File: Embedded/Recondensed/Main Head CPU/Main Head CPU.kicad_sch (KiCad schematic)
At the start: 52 parts, among them J1 10171746-00021LF, J10 Fan 1, J11 Substructure Power, J12 Head Power, J13 MicroSD, J14 Mic, J15 Expansion, J2 LEDs 0, J3 LEDs 1, J4 LEDs 2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

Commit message: Added LCSC Component IDs
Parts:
- removed SW1: Boot, Buttons:R-667843, symbol Switch:SW_Push
- removed SW2: RST, Buttons:R-667843, symbol Switch:SW_Push
- added S1: Boot, Buttons:SW_B3U-1000P, symbol Buttons:B3U-1000P
- added S2: RST, Buttons:SW_B3U-1000P, symbol Buttons:B3U-1000P
- C1, C4, C5: LCSC (none) -> C3039698
- C10, C2, C3, C8: LCSC (none) -> C1591
- C6: LCSC (none) -> C95843
- C7, C9: LCSC (none) -> C84419
- D1, D2: LCSC (none) -> C7207730
- D3: LCCS (none) -> C50603
- J1: footprint USBC:AMPHENOL_10171746-00021LF -> USBC:MOLEX_2171790001; LCSC (none) -> C3197684
- J10, J9: LCSC (none) -> C189893
- J13: LCSC (none) -> C587826
- J14, J15, J8: LCSC (none) -> C265111
- J2, J3, J4, J5, J6, J7: LCSC (none) -> C514175
- R1, R2: LCSC (none) -> C328432
- R10, R11, R12, R13, R14, R3, R5, R9: LCSC (none) -> C98220
- R7: value 155ohm min -> 145ohm; LCSC (none) -> C2930065
- R8: value 70ohm min -> 33ohm; LCSC (none) -> C108661
- U3: LCSC (none) -> C86781
- U4: LCSC (none) -> C134077
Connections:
- net GND: now also J1.A1B12 (GND_A), J1.B1A12 (GND_B), S1.2, S2.1; no longer J1.A1_B12 (GND_A), J1.B1_A12 (GND_B)
- net at C1.1, D3.A: now also J1.A4B9 (VBUS_A), J1.B4A9 (VBUS_B); no longer J1.A4_B9 (VBUS_A), J1.B4_A9 (VBUS_B)
- net at ESP1.27 (GPIO0/BOOT), R10.2: now also S1.1
- net at C6.2, ESP1.3 (EN), R9.2: now also S2.2
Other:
- moved on the sheet: J10, J9, Q1, Q2, R4, R6

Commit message: Modified Tables per component to centralise LCSC IDs
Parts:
- D3: LCCS C50603 -> (none); LCSC (none) -> C50603
- ESP1, J11, J12, U5: now left out of the parts list
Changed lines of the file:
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@@
 		(unit 1)
 		(exclude_from_sim no)
-		(in_bom yes)
+		(in_bom no)
 		(on_board yes)
 		(dnp no)
@@
 			)
 		)
-		(property "PARTREV" "A"
+		(property "LCSC" "C3197684"
 			(at 31.75 50.8 0)
 			(effects
@@
 					(size 1.27 1.27)
 				)
-				(justify bottom)
 				(hide yes)
 			)
 		)
-		(property "STANDARD" "Manufacturer Recommendations"
+		(property "PARTREV" "A"
 			(at 31.75 50.8 0)
 			(effects
@@
 			)
 		)
-		(property "MAXIMUM_PACKAGE_HEIGHT" "3.16 mm"
+		(property "STANDARD" "Manufacturer Recommendations"
 			(at 31.75 50.8 0)
 			(effects
@@
 			)
 		)
-		(property "MANUFACTURER" "Amphenol"
+		(property "MAXIMUM_PACKAGE_HEIGHT" "3.16 mm"
 			(at 31.75 50.8 0)
 			(effects
@@
 			)
 		)
-		(property "LCSC" "C3197684"
+		(property "MANUFACTURER" "Amphenol"
 			(at 31.75 50.8 0)
 			(effects
@@
 					(size 1.27 1.27)
 				)
+				(justify bottom)
 				(hide yes)
 			)
@@
 			)
 		)
-		(property "Sim.Device" ""
+		(property "LCSC" "C514175"
 			(at 38.1 129.54 0)
 			(effects
@@
 			)
 		)
-		(property "Sim.Pins" ""
+		(property "Sim.Device" ""
 			(at 38.1 129.54 0)
 			(effects
@@
 			)
 		)
-		(property "LCSC" "C514175"
+		(property "Sim.Pins" ""
 			(at 38.1 129.54 0)
 			(effects
@@
 			)
 		)
-		(property "Sim.Device" ""
+		(property "LCSC" "C514175"
 			(at 38.1 104.14 0)
 			(effects
@@
 			)
 		)
-		(property "Sim.Pins" ""
+		(property "Sim.Device" ""
 			(at 38.1 104.14 0)
 			(effects
@@
 			)
 		)
-		(property "LCSC" "C514175"
+		(property "Sim.Pins" ""
 			(at 38.1 104.14 0)
 			(effects
@@
 			)
 		)
+		(property "LCSC" "C231329 "
+			(at 262.89 59.69 90)
+			(effects
+				(font
+					(size 1.27 1.27)
+				)
+				(hide yes)
+			)
+		)
 		(property "MF" "Omron"
 			(at 262.89 59.69 0)
@@
 			)
 		)
-		(property "LCSC" "C231329 "
-			(at 262.89 59.69 90)
-			(effects
-				(font
-					(size 1.27 1.27)
-				)
-				(hide yes)
-			)
-		)
 		(pin "2"
 		)
@@
 		(unit 1)
 		(exclude_from_sim no)
-		(in_bom yes)
+		(in_bom no)
 		(on_board yes)
 		(dnp no)
@@
 			)
 		)
-		(property "Sim.Device" ""
+		(property "LCSC" "C514175"
 			(at 38.1 142.24 0)
 			(effects
@@
 			)
 		)
-		(property "Sim.Pins" ""
+		(property "Sim.Device" ""
 			(at 38.1 142.24 0)
 			(effects
@@
 			)
 		)
-		(property "LCSC" "C514175"
+		(property "Sim.Pins" ""
 			(at 38.1 142.24 0)
 			(effects
@@
 			)
 		)
+		(property "LCSC" "C231329 "
+			(at 392.43 74.93 90)
+			(effects
+				(font
+					(size 1.27 1.27)
+				)
+				(hide yes)
+			)
+		)
 		(property "MF" "Omron"
 			(at 392.43 74.93 0)
@@
 			)
 		)
-		(property "LCSC" "C231329 "
-			(at 392.43 74.93 90)
-			(effects
-				(font
-					(size 1.27 1.27)
-				)
-				(hide yes)
-			)
-		)
 		(pin "2"
 		)
@@
 		(unit 1)
 		(exclude_from_sim no)
-		(in_bom yes)
+		(in_bom no)
 		(on_board yes)
 		(dnp no)
@@
 			)
 		)
-		(property "Sim.Device" ""
+		(property "LCSC" "C514175"
 			(at 38.1 167.64 0)
 			(effects
@@
 			)
 		)
-		(property "Sim.Pins" ""
+		(property "Sim.Device" ""
 			(at 38.1 167.64 0)
 			(effects
@@
 			)
 		)
-		(property "LCSC" "C514175"
+		(property "Sim.Pins" ""
 			(at 38.1 167.64 0)
 			(effects
@@
 			)
 		)
-		(property "Sim.Device" ""
+		(property "LCSC" "C514175"
 			(at 38.1 154.94 0)
 			(effects
@@
 			)
 		)
-		(property "Sim.Pins" ""
+		(property "Sim.Device" ""
 			(at 38.1 154.94 0)
 			(effects
@@
 			)
 		)
-		(property "LCSC" "C514175"
+		(property "Sim.Pins" ""
 			(at 38.1 154.94 0)
 			(effects
@@
 		(unit 1)
 		(exclude_from_sim no)
-		(in_bom yes)
+		(in_bom no)
 		(on_board yes)
 		(dnp no)
@@
 			)
 		)
-		(property "Sim.Device" ""
+		(property "LCSC" "C514175"
 			(at 38.1 116.84 0)
 			(effects
@@
 			)
 		)
-		(property "Sim.Pins" ""
+		(property "Sim.Device" ""
 			(at 38.1 116.84 0)
 			(effects
@@
 			)
 		)
-		(property "LCSC" "C514175"
+		(property "Sim.Pins" ""
 			(at 38.1 116.84 0)
 			(effects
@@
 			)
 		)
-		(property "MF" "Nexperia USA Inc."
+		(property "LCSC" "C50603"
 			(at 82.55 39.37 0)
 			(effects
@@
 					(size 1.27 1.27)
 				)
-				(justify bottom)
 				(hide yes)
 			)
 		)
-		(property "DESCRIPTION" "Diode Schottky 30 V 5A Surface Mount SOD-128/CFP5"
+		(property "MF" "Nexperia USA Inc."
 			(at 82.55 39.37 0)
 			(effects
@@
 			)
 		)
-		(property "PACKAGE" "SOD-128 Nexperia USA Inc."
+		(property "DESCRIPTION" "Diode Schottky 30 V 5A Surface Mount SOD-128/CFP5"
 			(at 82.55 39.37 0)
 			(effects
@@
 			)
 		)
-		(property "PRICE" "None"
+		(property "PACKAGE" "SOD-128 Nexperia USA Inc."
 			(at 82.55 39.37 0)
 			(effects
@@
 			)
 		)
-		(property "MP" "PMEG3050EP,115"
+		(property "PRICE" "None"
 			(at 82.55 39.37 0)
 			(effects
@@
 			)
 		)
-		(property "AVAILABILITY" "In Stock"
+		(property "MP" "PMEG3050EP,115"
 			(at 82.55 39.37 0)
 			(effects
@@
 			)
 		)
-		(property "PURCHASE-URL" "https://pricing.snapeda.com/search/part/PMEG3050EP,115/?ref=eda"
+		(property "AVAILABILITY" "In Stock"
 			(at 82.55 39.37 0)
 			(effects
@@
 			)
 		)
-		(property "LCCS" "C50603"
+		(property "PURCHASE-URL" "https://pricing.snapeda.com/search/part/PMEG3050EP,115/?ref=eda"
 			(at 82.55 39.37 0)
 			(effects
@@
 					(size 1.27 1.27)
 				)
+				(justify bottom)
 				(hide yes)
 			)

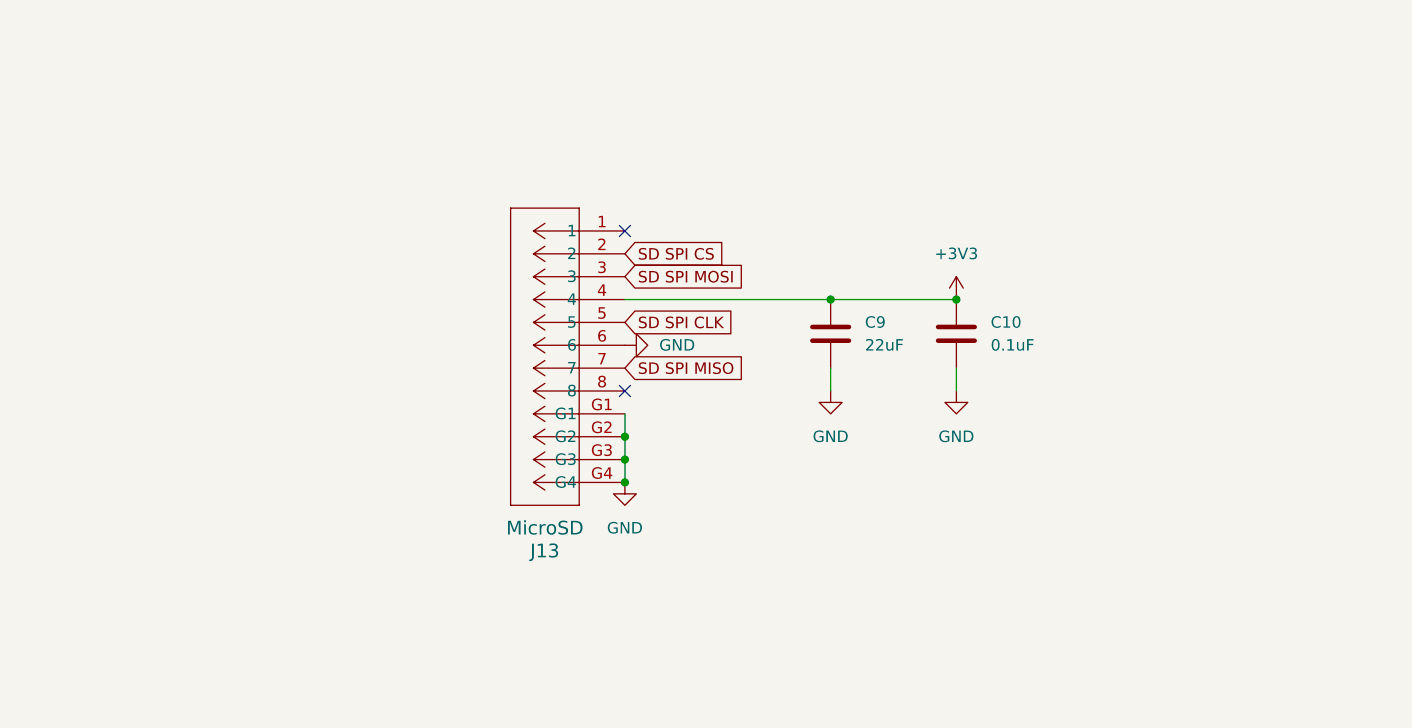
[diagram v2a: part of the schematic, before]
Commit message: Added Pullups for MicroSD & Modified Silkscreen
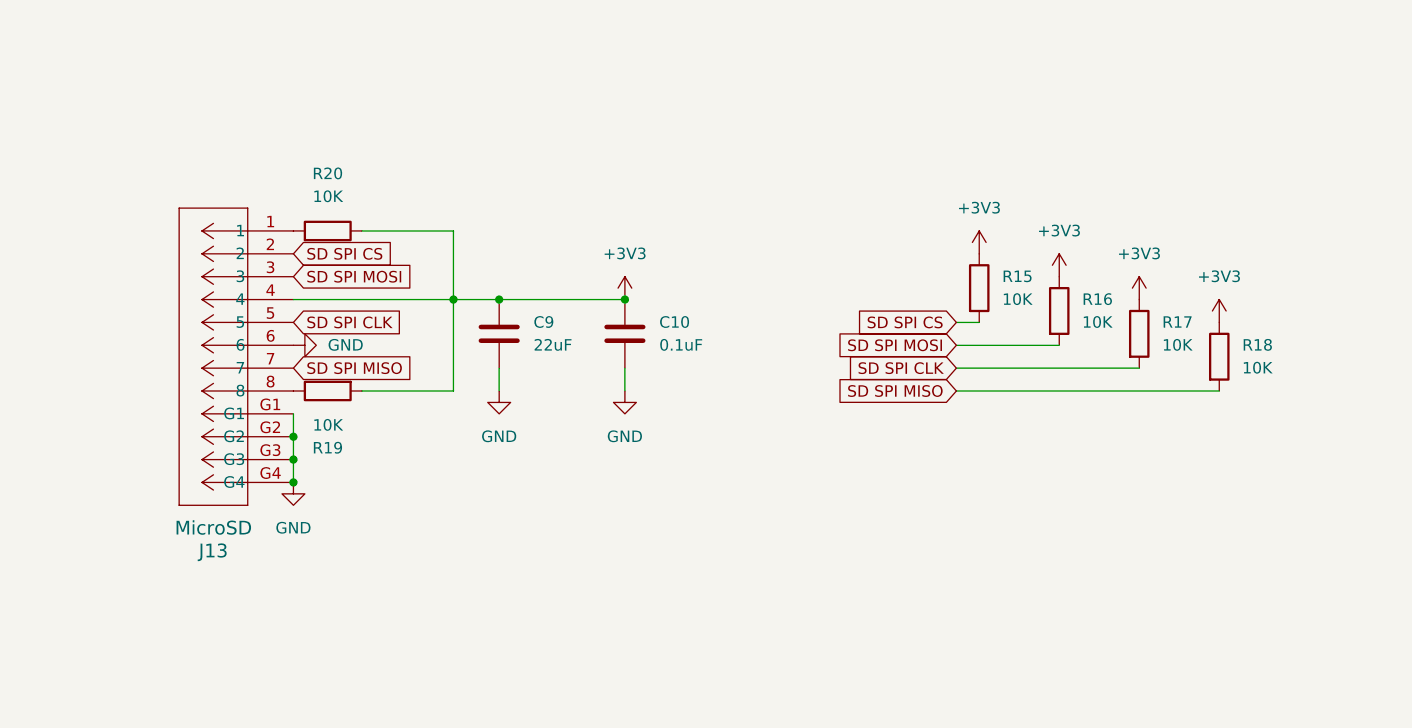
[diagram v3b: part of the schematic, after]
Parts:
- added R15, R16, R17, R18, R19, R20: 10K, Resistor_SMD:R_0603_1608Metric_Pad0.98x0.95mm_HandSolder, symbol Device:R
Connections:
- net +3V3: now also R15.1, R16.1, R17.1, R18.1, R19.2, R20.1
- net SD SPI CLK: now also R17.2
- net SD SPI CS: now also R15.2
- net SD SPI MISO: now also R18.2
- net SD SPI MOSI: now also R16.2
- net at J13.1: now also R20.2
- net at J13.8: now also R19.1
- no-connect marks 11 -> 9
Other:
- moved on the sheet: C10, C9, J13
